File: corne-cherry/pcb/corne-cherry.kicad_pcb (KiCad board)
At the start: 2 copper layers, 133.8 x 91.4 mm, 98 parts, among them J3 LED, P1 i2c-pin, P2 i2c-pin, SW1 SW_PUSH, SW10 SW_PUSH, SW11 SW_PUSH, SW12 SW_PUSH, SW13 SW_PUSH, SW14 SW_PUSH, SW15 SW_PUSH, SW16 SW_PUSH, SW17 SW_PUSH, SW18 SW_PUSH, SW19 SW_PUSH, SW2 SW_PUSH, SW20 SW_PUSH, SW21 SW_PUSH, SW3 SW_PUSH, SW4 SW_PUSH, SW5 SW_PUSH, SW6 SW_PUSH, SW7 SW_PUSH, SW8 SW_PUSH, SW9 SW_PUSH, U1 ProMicro

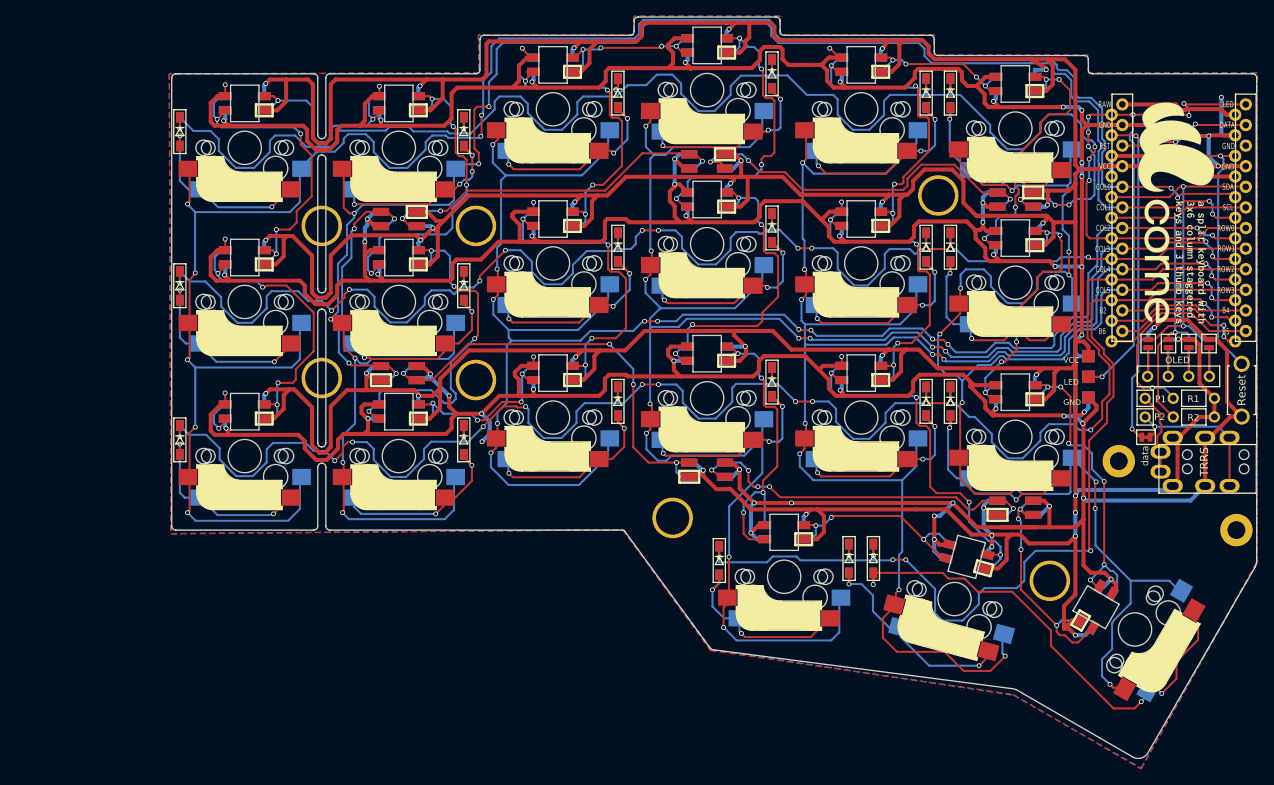
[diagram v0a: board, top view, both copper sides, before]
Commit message: fixed corne-cherry outlines
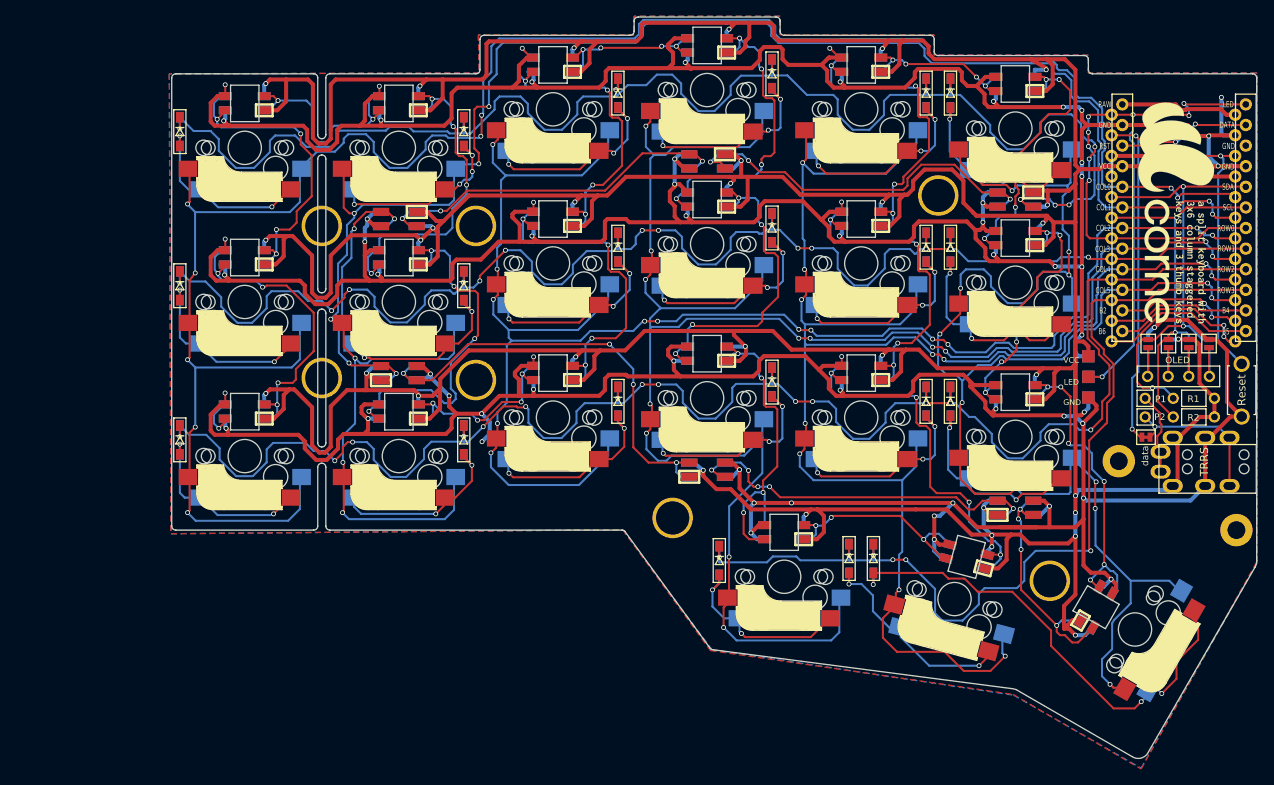
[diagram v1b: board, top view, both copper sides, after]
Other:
- outline, holes or cut-outs redrawn
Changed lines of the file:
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@@
-(kicad_pcb (version 20171130) (host pcbnew "(5.0.0-3-g5ebb6b6)")
+(kicad_pcb (version 20171130) (host pcbnew "(5.1.0)-1")
   (general
     (thickness 1.6)
@@
     (zone_45_only no)
     (trace_min 0.2)
-    (segment_width 0.1)
-    (edge_width 0.15)
     (via_size 0.6)
     (via_drill 0.4)
@@
     (uvia_min_size 0.2)
     (uvia_min_drill 0.1)
+    (edge_width 0.15)
+    (segment_width 0.1)
     (pcb_text_width 0.3)
     (pcb_text_size 1.5 1.5)
@@
     (pad_to_mask_clearance 0.2)
     (aux_axis_origin 194.75 68)
-    (visible_elements FFFFFF7F)
+    (grid_origin 106.25 69.15)
+    (visible_elements 7FFFFFFF)
     (pcbplotparams
       (layerselection 0x010f0_ffffffff)
@@
   (gr_arc (start 180.14425 151.010957) (end 179.369251 152.160956) (angle -90.22347501) (layer Edge.Cuts) (width 0.15))
   (gr_arc (start 164.087404 147.16844) (end 165.075 143.9) (angle -11.21335546) (layer Edge.Cuts) (width 0.15))
-  (gr_line (start 181.3 151.775) (end 194.525 128.85) (layer Edge.Cuts) (width 0.15))
-  (gr_line (start 165.075 143.9) (end 179.4 152.175) (layer Edge.Cuts) (width 0.15))
-  (gr_line (start 127.75 139) (end 164.45 143.775) (layer Edge.Cuts) (width 0.15))
+  (gr_line (start 181.297263 151.781465) (end 194.525 128.85) (layer Edge.Cuts) (width 0.15))
+  (gr_line (start 165.075 143.9) (end 179.369251 152.160956) (layer Edge.Cuts) (width 0.15))
+  (gr_line (start 127.75 139) (end 164.420556 143.770344) (layer Edge.Cuts) (width 0.15))
   (gr_arc (start 127.75 138.5) (end 127.75 139) (angle 45) (layer Edge.Cuts) (width 0.15))
-  (gr_line (start 116.85 124.4) (end 127.4 138.85) (angle 90) (layer Edge.Cuts) (width 0.15))
+  (gr_line (start 116.853553 124.396447) (end 127.396447 138.853553) (angle 90) (layer Edge.Cuts) (width 0.15))
   (gr_text OLED (at 185.1 103.3) (layer B.SilkS)
     (effects (font (size 0.8128 0.8128) (thickness 0.15)) (justify mirror))
@@
   (gr_line (start 138.25 126.75) (end 138.25 122.3) (angle 90) (layer Edge.Cuts) (width 0.15))
   (gr_line (start 134.75 126.75) (end 138.25 126.75) (angle 90) (layer Edge.Cuts) (width 0.15))
-  (gr_line (start 134.75 122.35) (end 134.75 126.75) (angle 90) (layer Edge.Cuts) (width 0.15))
+  (gr_line (start 134.75 122.3) (end 134.75 126.75) (angle 90) (layer Edge.Cuts) (width 0.15))
   (gr_line (start 166.75 105) (end 163.25 105) (angle 90) (layer Edge.Cuts) (width 0.15))
   (gr_line (start 166.75 109.5) (end 166.75 105) (angle 90) (layer Edge.Cuts) (width 0.15))
@@
   (gr_line (start 147.75 107.15) (end 147.75 102.65) (angle 90) (layer Edge.Cuts) (width 0.15))
   (gr_line (start 144.25 107.15) (end 147.75 107.15) (angle 90) (layer Edge.Cuts) (width 0.15))
-  (gr_line (start 144.25 102.65) (end 144.25 107.1) (angle 90) (layer Edge.Cuts) (width 0.15))
+  (gr_line (start 144.25 102.65) (end 144.25 107.15) (angle 90) (layer Edge.Cuts) (width 0.15))
   (gr_line (start 128.75 100.25) (end 125.25 100.25) (angle 90) (layer Edge.Cuts) (width 0.15))
-  (gr_line (start 128.75 104.75) (end 128.75 100.3) (angle 90) (layer Edge.Cuts) (width 0.15))
+  (gr_line (start 128.75 104.75) (end 128.75 100.25) (angle 90) (layer Edge.Cuts) (width 0.15))
   (gr_line (start 125.25 104.75) (end 128.75 104.75) (angle 90) (layer Edge.Cuts) (width 0.15))
-  (gr_line (start 125.25 100.3) (end 125.25 104.75) (angle 90) (layer Edge.Cuts) (width 0.15))
+  (gr_line (start 125.25 100.25) (end 125.25 104.75) (angle 90) (layer Edge.Cuts) (width 0.15))
   (gr_line (start 109.75 102.65) (end 106.25 102.65) (angle 90) (layer Edge.Cuts) (width 0.15))
   (gr_line (start 109.75 107.15) (end 109.75 102.65) (angle 90) (layer Edge.Cuts) (width 0.15))
   (gr_line (start 106.25 107.15) (end 109.75 107.15) (angle 90) (layer Edge.Cuts) (width 0.15))
-  (gr_line (start 106.25 102.65) (end 106.25 107.1) (angle 90) (layer Edge.Cuts) (width 0.15))
+  (gr_line (start 106.25 102.65) (end 106.25 107.15) (angle 90) (layer Edge.Cuts) (width 0.15))
   (gr_line (start 166.75 86) (end 163.25 86) (angle 90) (layer Edge.Cuts) (width 0.15))
   (gr_line (start 166.75 90.5) (end 166.75 86) (angle 90) (layer Edge.Cuts) (width 0.15))
@@
   (gr_line (start 147.75 88.15) (end 147.75 83.65) (angle 90) (layer Edge.Cuts) (width 0.15))
   (gr_line (start 144.25 88.15) (end 147.75 88.15) (angle 90) (layer Edge.Cuts) (width 0.15))
-  (gr_line (start 144.25 83.65) (end 144.25 88.1) (angle 90) (layer Edge.Cuts) (width 0.15))
+  (gr_line (start 144.25 83.65) (end 144.25 88.15) (angle 90) (layer Edge.Cuts) (width 0.15))
   (gr_line (start 128.75 81.25) (end 125.25 81.25) (angle 90) (layer Edge.Cuts) (width 0.15))
-  (gr_line (start 128.75 85.75) (end 128.75 81.3) (angle 90) (layer Edge.Cuts) (width 0.15))
+  (gr_line (start 128.75 85.75) (end 128.75 81.25) (angle 90) (layer Edge.Cuts) (width 0.15))
   (gr_line (start 125.25 85.75) (end 128.75 85.75) (angle 90) (layer Edge.Cuts) (width 0.15))
-  (gr_line (start 125.25 81.3) (end 125.25 85.75) (angle 90) (layer Edge.Cuts) (width 0.15))
+  (gr_line (start 125.25 81.25) (end 125.25 85.75) (angle 90) (layer Edge.Cuts) (width 0.15))
   (gr_line (start 109.75 83.65) (end 106.25 83.65) (angle 90) (layer Edge.Cuts) (width 0.15))
   (gr_line (start 109.75 88.15) (end 109.75 83.65) (angle 90) (layer Edge.Cuts) (width 0.15))
   (gr_line (start 106.25 88.15) (end 109.75 88.15) (angle 90) (layer Edge.Cuts) (width 0.15))
-  (gr_line (start 106.25 83.65) (end 106.25 88.1) (angle 90) (layer Edge.Cuts) (width 0.15))
+  (gr_line (start 106.25 83.65) (end 106.25 88.15) (angle 90) (layer Edge.Cuts) (width 0.15))
   (gr_line (start 166.75 67) (end 163.25 67) (angle 90) (layer Edge.Cuts) (width 0.15))
   (gr_line (start 166.75 71.5) (end 166.75 67) (angle 90) (layer Edge.Cuts) (width 0.15))
@@
   (gr_line (start 147.75 69.15) (end 147.75 64.65) (angle 90) (layer Edge.Cuts) (width 0.15))
   (gr_line (start 144.25 69.15) (end 147.75 69.15) (angle 90) (layer Edge.Cuts) (width 0.15))
-  (gr_line (start 144.25 64.65) (end 144.25 69.1) (angle 90) (layer Edge.Cuts) (width 0.15))
+  (gr_line (start 144.25 64.65) (end 144.25 69.15) (angle 90) (layer Edge.Cuts) (width 0.15))
   (gr_line (start 128.75 62.25) (end 125.25 62.25) (angle 90) (layer Edge.Cuts) (width 0.15))
   (gr_line (start 128.75 66.75) (end 128.75 62.25) (angle 90) (layer Edge.Cuts) (width 0.15))
   (gr_line (start 125.25 66.75) (end 128.75 66.75) (angle 90) (layer Edge.Cuts) (width 0.15))
-  (gr_line (start 125.25 62.25) (end 125.25 66.7) (angle 90) (layer Edge.Cuts) (width 0.15))
+  (gr_line (start 125.25 62.25) (end 125.25 66.75) (angle 90) (layer Edge.Cuts) (width 0.15))
   (gr_line (start 109.75 64.65) (end 106.25 64.65) (angle 90) (layer Edge.Cuts) (width 0.15))
   (gr_line (start 109.75 69.15) (end 109.75 64.65) (angle 90) (layer Edge.Cuts) (width 0.15))
   (gr_line (start 106.25 69.15) (end 109.75 69.15) (angle 90) (layer Edge.Cuts) (width 0.15))
-  (gr_line (start 106.25 64.65) (end 106.25 69.1) (angle 90) (layer Edge.Cuts) (width 0.15))
+  (gr_line (start 106.25 64.65) (end 106.25 69.15) (angle 90) (layer Edge.Cuts) (width 0.15))
   (gr_line (start 90.75 107.4) (end 87.25 107.4) (angle 90) (layer Edge.Cuts) (width 0.15))
   (gr_line (start 90.75 111.9) (end 90.75 107.4) (angle 90) (layer Edge.Cuts) (width 0.15))

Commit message: added drawings
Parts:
- added D22: D, kbd:D3_SMD, F.Cu at (43.0, 89.4)
- added L28: SK6812MINI, kbd:SK6812MINI_rev, F.Cu at (51.0, 85.9)
- added SW22: SW_PUSH, kbd:CherryMX_MidHeight_Hotswap, F.Cu at (51.0, 91.4)
- G01, G02: renamed from G***; value LOGO -> Logo_Open_Hardware_Small
- H1, H2, H3, H4, H5, H6, H7, H8, H9: renamed from ?; value (none) -> MountingHole
- RSW1: value Reset -> SW_PUSH
- renumbered TRRS to J1, OLED to J2, data to JP1
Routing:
- net row3: track 119.7 -> 239.1 mm, vias 6 -> 10
- net Net-(L13-Pad1): track 5.40 -> 37.8 mm, vias 1 -> 4
- net col0: track 250.8 -> 280.0 mm, vias 9 -> 10
- net Net-(D22-Pad2): track 0.00 -> 27.4 mm, vias 0 -> 1
- net GND: track 828.4 -> 855.0 mm, vias 61 -> 62
- net VCC: track 759.2 -> 784.8 mm, vias 33 -> 34
- net Net-(D21-Pad2): track 61.1 -> 69.1 mm, vias 3 -> 2
- net col1: track 233.4 -> 237.6 mm
- net Net-(L28-Pad1): track 0.00 -> 4.19 mm, vias 0 -> 1
- net col4: track 203.2 -> 207.1 mm
- net col5: track 188.2 -> 191.8 mm
- net col2: track 202.1 -> 205.6 mm
- net col3: track 228.9 -> 232.2 mm
- net Net-(L19-Pad3): track 27.9 -> 28.8 mm
- net Net-(D4-Pad2): track 24.5 -> 25.4 mm
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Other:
- board size 133.8 x 91.4 mm -> 152.8 x 91.4 mm
- board text added: "Jorne Cherry v2.1 PCB Designed by Joric"
- board text removed: "Corne Cherry v2.1 PCB Designed by foostan"
